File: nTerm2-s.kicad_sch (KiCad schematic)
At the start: 107 parts, among them J1 VGA, J2 Keyboard, J3 Mouse, J4 Speaker, J5 DE9_Plug_MountingHoles, J6 USB_C_Receptacle_USB2.0_16P, K1 IM41 3V, K2 IM41 3V, K3 IM41 3V, Q1 BC817, Q2 BC817, Q3 BC817, Q4 BC817, Q5 BC817, SW1 IO0, SW2 RESET, SW3 DEFAULTS, U1 ESP32-WROOM-32, U2 LM386, U3 MAX3232E, U4 CP2102N-Axx-xQFN28, U5 NCP1117-3.3_SOT223

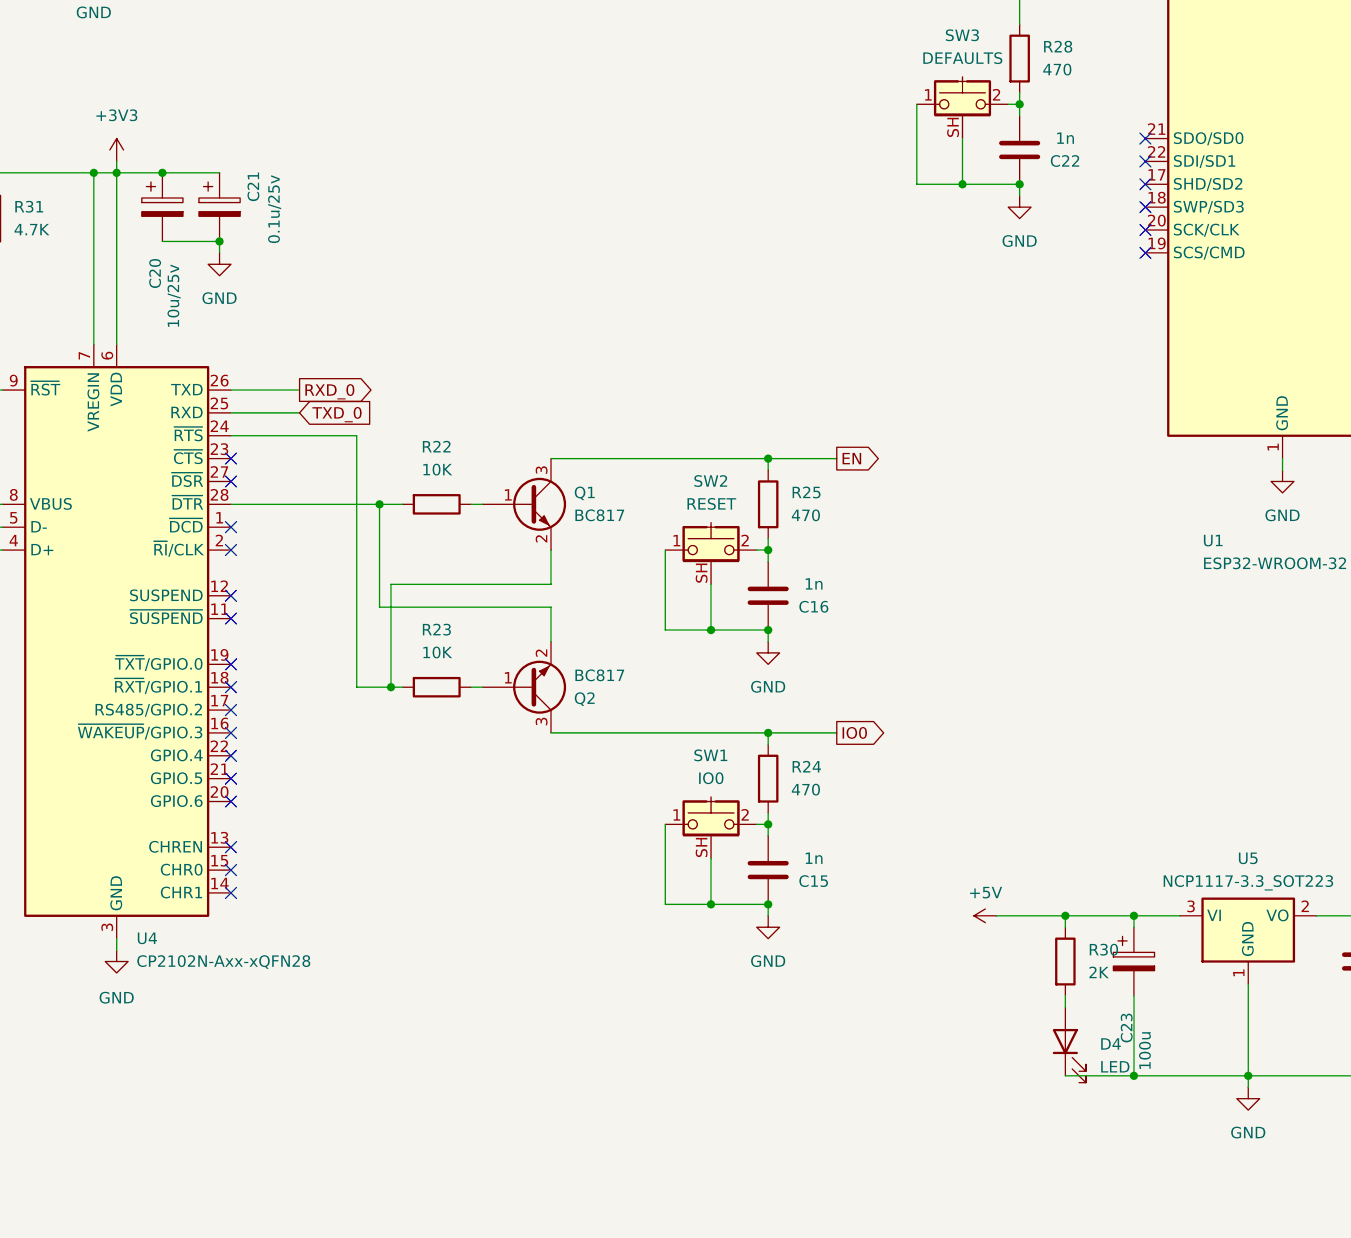
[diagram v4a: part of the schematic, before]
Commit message: Fix all tantalum capacitor sizes.
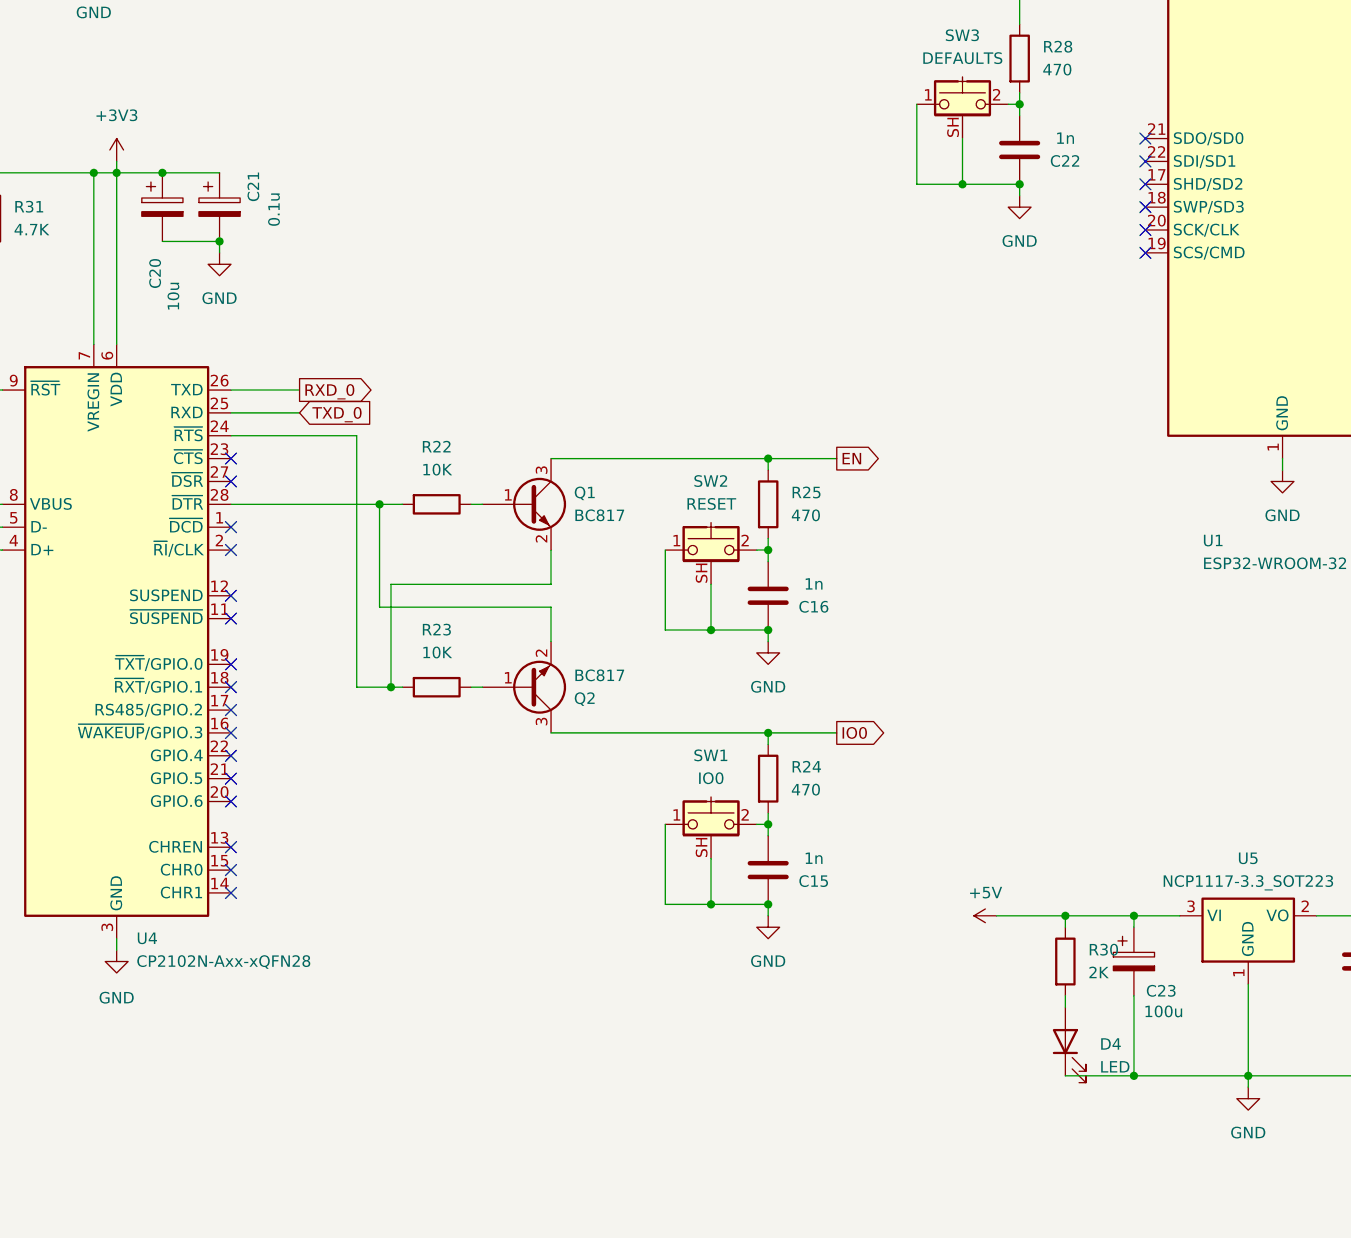
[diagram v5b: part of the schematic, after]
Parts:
- C13, C18, C23: footprint Capacitor_Tantalum_SMD:CP_EIA-3216-18_Kemet-A_Pad1.58x1.35mm_HandSolder -> Capacitor_Tantalum_SMD:CP_EIA-6032-28_Kemet-C_Pad2.25x2.35mm_HandSolder
- C20: value 10u/25v -> 10u; footprint Capacitor_Tantalum_SMD:CP_EIA-3216-18_Kemet-A_Pad1.58x1.35mm_HandSolder -> Capacitor_Tantalum_SMD:CP_EIA-3528-21_Kemet-B_Pad1.50x2.35mm_HandSolder
- C21: value 0.1u/25v -> 0.1u
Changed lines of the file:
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@@
 			)
 		)
-		(property "Value" "0.1u/25v"
+		(property "Value" "0.1u"
 			(at 125.476 75.184 90)
 			(effects
@@
 			)
 		)
-		(property "Value" "10u/25v"
+		(property "Value" "10u"
 			(at 114.3 84.836 90)
 			(effects
@@
 			)
 		)
-		(property "Footprint" "Capacitor_Tantalum_SMD:CP_EIA-3216-18_Kemet-A_Pad1.58x1.35mm_HandSolder"
+		(property "Footprint" "Capacitor_Tantalum_SMD:CP_EIA-3528-21_Kemet-B_Pad1.50x2.35mm_HandSolder"
 			(at 113.9952 78.74 0)
 			(effects
@@
 			)
 		)
-		(property "Footprint" "Capacitor_Tantalum_SMD:CP_EIA-3216-18_Kemet-A_Pad1.58x1.35mm_HandSolder"
+		(property "Footprint" "Capacitor_Tantalum_SMD:CP_EIA-6032-28_Kemet-C_Pad2.25x2.35mm_HandSolder"
 			(at 63.1952 133.35 0)
 			(effects
@@
 			)
 		)
-		(property "Footprint" "Capacitor_Tantalum_SMD:CP_EIA-3216-18_Kemet-A_Pad1.58x1.35mm_HandSolder"
+		(property "Footprint" "Capacitor_Tantalum_SMD:CP_EIA-6032-28_Kemet-C_Pad2.25x2.35mm_HandSolder"
 			(at 271.4752 31.75 0)
 			(effects
@@
 		(dnp no)
 		(property "Reference" "C23"
-			(at 220.218 166.116 90)
+			(at 224.028 162.052 0)
 			(effects
 				(font
@@
 		)
 		(property "Value" "100u"
-			(at 222.25 168.656 90)
+			(at 224.282 164.338 0)
 			(effects
 				(font
@@
 			)
 		)
-		(property "Footprint" "Capacitor_Tantalum_SMD:CP_EIA-3216-18_Kemet-A_Pad1.58x1.35mm_HandSolder"
+		(property "Footprint" "Capacitor_Tantalum_SMD:CP_EIA-6032-28_Kemet-C_Pad2.25x2.35mm_HandSolder"
 			(at 221.9452 162.56 0)
 			(effects

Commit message: Some small replacements, doublechecked size of tiny ESD protectors, but they are really *tiny*. Set them further apart, so maybe they are easier to solder this way.
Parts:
- D1, D2: footprint Diode_SMD:D_SOD-923 -> ESD9D5.0ST5G:TVS_ESD9D5.0ST5G
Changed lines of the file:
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@@
 			)
 		)
-		(property "Footprint" "Diode_SMD:D_SOD-923"
+		(property "Footprint" "ESD9D5.0ST5G:TVS_ESD9D5.0ST5G"
 			(at 52.07 129.54 0)
 			(effects
@@
 			)
 		)
-		(property "Footprint" "Diode_SMD:D_SOD-923"
+		(property "Footprint" "ESD9D5.0ST5G:TVS_ESD9D5.0ST5G"
 			(at 57.15 129.54 0)
 			(effects

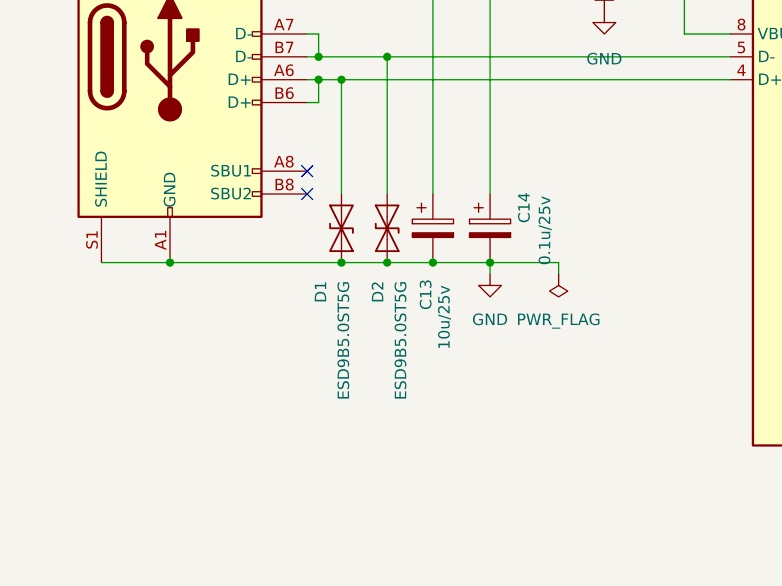
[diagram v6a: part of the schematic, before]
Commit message: Use other TVS protection diodes, with a hand-solderable size.
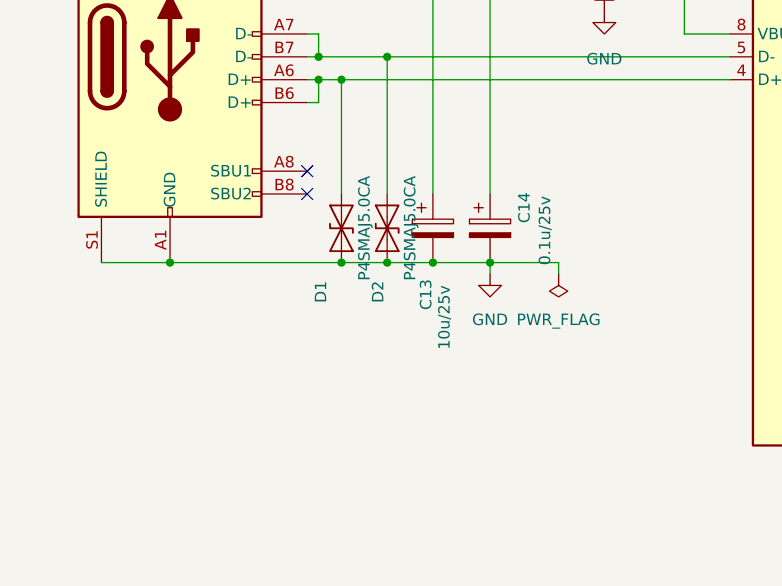
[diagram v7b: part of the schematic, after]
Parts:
- D1, D2: value ESD9B5.0ST5G -> P4SMAJ5.0CA; footprint ESD9D5.0ST5G:TVS_ESD9D5.0ST5G -> Diode_SMD:D_SMA_Handsoldering; symbol Diode:ESD9B5.0ST5G -> Diode:P4SMAJ5.0CA
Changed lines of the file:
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@@
 	)
 	(symbol
-		(lib_id "Diode:ESD9B5.0ST5G")
+		(lib_id "Diode:P4SMAJ5.0CA")
 		(at 52.07 129.54 90)
 		(unit 1)
@@
 			)
 		)
-		(property "Value" "ESD9B5.0ST5G"
-			(at 52.324 135.382 0)
+		(property "Value" "P4SMAJ5.0CA"
+			(at 54.61 129.54 0)
 			(effects
 				(font
 					(size 1.27 1.27)
 				)
-				(justify right)
 			)
 		)
-		(property "Footprint" "ESD9D5.0ST5G:TVS_ESD9D5.0ST5G"
+		(property "Footprint" "Diode_SMD:D_SMA_Handsoldering"
 			(at 52.07 129.54 0)
 			(effects
@@
 	)
 	(symbol
-		(lib_id "Diode:ESD9B5.0ST5G")
+		(lib_id "Diode:P4SMAJ5.0CA")
 		(at 57.15 129.54 90)
 		(unit 1)
@@
 			)
 		)
-		(property "Value" "ESD9B5.0ST5G"
-			(at 58.674 135.382 0)
+		(property "Value" "P4SMAJ5.0CA"
+			(at 59.69 129.54 0)
 			(effects
 				(font
 					(size 1.27 1.27)
 				)
-				(justify right)
 			)
 		)
-		(property "Footprint" "ESD9D5.0ST5G:TVS_ESD9D5.0ST5G"
+		(property "Footprint" "Diode_SMD:D_SMA_Handsoldering"
 			(at 57.15 129.54 0)
 			(effects

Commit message: More small improvements to layout.
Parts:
- C25, C26, C27: footprint Capacitor_Tantalum_SMD:CP_EIA-3216-18_Kemet-A_Pad1.58x1.35mm_HandSolder -> Capacitor_SMD:CP_Elec_6.3x7.7
- D1, D2: footprint Diode_SMD:D_SMA_Handsoldering -> Diode_SMD:D_SMA
- K1, K2, K3: footprint Relay_SMD:Relay_2P2T_10x6mm_TE_IMxxG -> Relay_SMD:Relay_DPDT_AXICOM_IMSeries_Gullwing
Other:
- company: Sporos Tech -> Sporos Tech ₍^•_•^₎ﾉ
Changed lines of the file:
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@@
 	(title_block
 		(title "nTerm2-s")
-		(date "2025-01-15")
+		(date "2025-01-30")
 		(rev "0.03")
-		(company "Sporos Tech")
-		(comment 1 "© 2025 Sporos Tech ₍^•_•^₎ﾉ")
-		(comment 2 "Peter de Vroomen")
+		(company "Sporos Tech ₍^•_•^₎ﾉ")
+		(comment 1 "Peter de Vroomen")
+		(comment 2 "© 2025 Sporos Tech ₍^•_•^₎ﾉ")
 	)
 	(junction
@@
 		)
 		(property "Value" "P4SMAJ5.0CA"
-			(at 54.61 129.54 0)
+			(at 51.816 141.732 0)
 			(effects
 				(font
@@
 			)
 		)
-		(property "Footprint" "Diode_SMD:D_SMA_Handsoldering"
+		(property "Footprint" "Diode_SMD:D_SMA"
 			(at 52.07 129.54 0)
 			(effects
@@
 			)
 		)
-		(property "Footprint" "Capacitor_Tantalum_SMD:CP_EIA-3216-18_Kemet-A_Pad1.58x1.35mm_HandSolder"
+		(property "Footprint" "Capacitor_SMD:CP_Elec_6.3x7.7"
 			(at 360.68 143.8148 0)
 			(effects
@@
 			)
 		)
-		(property "Footprint" "Capacitor_Tantalum_SMD:CP_EIA-3216-18_Kemet-A_Pad1.58x1.35mm_HandSolder"
+		(property "Footprint" "Capacitor_SMD:CP_Elec_6.3x7.7"
 			(at 360.68 179.3748 0)
 			(effects
@@
 			)
 		)
-		(property "Footprint" "Relay_SMD:Relay_2P2T_10x6mm_TE_IMxxG"
+		(property "Footprint" "Relay_SMD:Relay_DPDT_AXICOM_IMSeries_Gullwing"
 			(at 195.58 252.73 0)
 			(effects
@@
 			)
 		)
-		(property "Footprint" "Capacitor_Tantalum_SMD:CP_EIA-3216-18_Kemet-A_Pad1.58x1.35mm_HandSolder"
+		(property "Footprint" "Capacitor_SMD:CP_Elec_6.3x7.7"
 			(at 360.68 214.9348 0)
 			(effects
@@
 			)
 		)
-		(property "Footprint" "Relay_SMD:Relay_2P2T_10x6mm_TE_IMxxG"
+		(property "Footprint" "Relay_SMD:Relay_DPDT_AXICOM_IMSeries_Gullwing"
 			(at 127 255.27 0)
 			(effects
@@
 		)
 		(property "Value" "P4SMAJ5.0CA"
-			(at 59.69 129.54 0)
+			(at 57.912 141.732 0)
 			(effects
 				(font
@@
 			)
 		)
-		(property "Footprint" "Diode_SMD:D_SMA_Handsoldering"
+		(property "Footprint" "Diode_SMD:D_SMA"
 			(at 57.15 129.54 0)
 			(effects
@@
 			)
 		)
-		(property "Footprint" "Relay_SMD:Relay_2P2T_10x6mm_TE_IMxxG"
+		(property "Footprint" "Relay_SMD:Relay_DPDT_AXICOM_IMSeries_Gullwing"
 			(at 127 220.98 0)
 			(effects
